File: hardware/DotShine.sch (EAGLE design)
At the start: 55 parts, among them CN1 1X4-BIG, IC1 CAT24M010TS, IC3 SI1145, J3 USB-MICROB, U1 ATMEGA328P-MU-QFN32, U2 TMP102, U3 ATSHA204-TSU, X2 MC-RTC-RV-4162-C7-I2C, X3 S4B-ZR

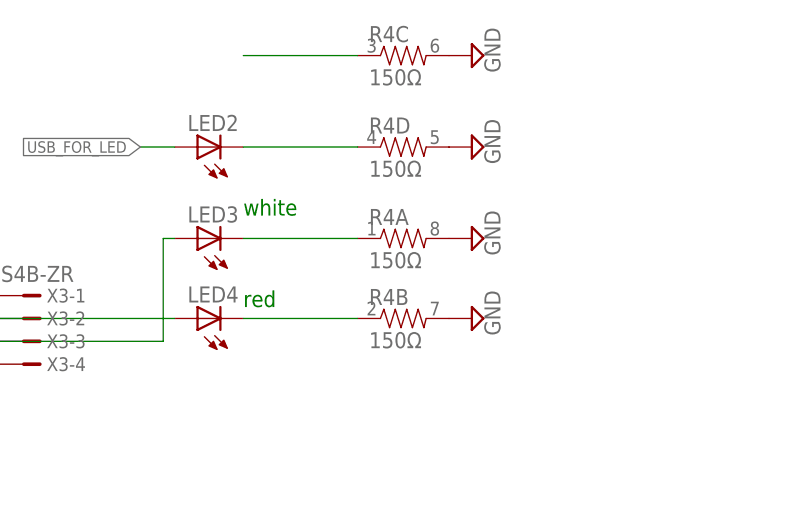
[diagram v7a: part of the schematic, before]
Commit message: Remove IXYS SLMD121H9L solar cell 45mA@4.5V, use small cell and i2c micro crystal
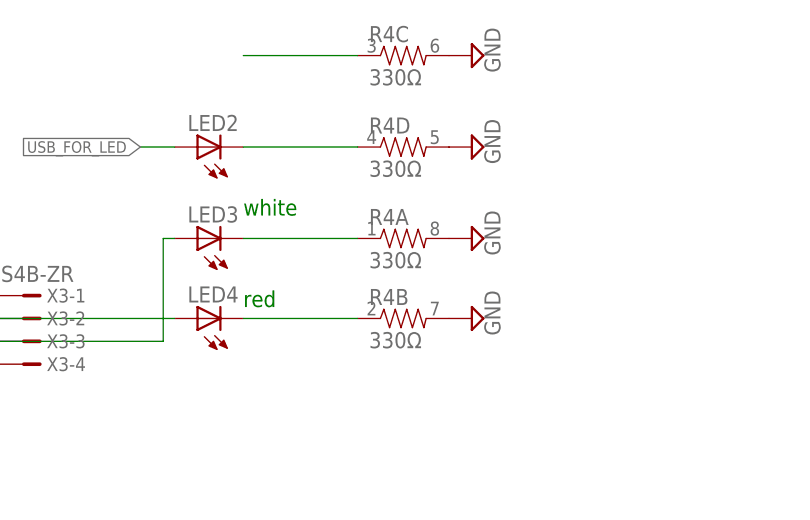
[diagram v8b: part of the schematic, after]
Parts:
- R4: value 150Ω -> 330Ω
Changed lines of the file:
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@@
 <setting verticaltext="up"/>
 </settings>
-<grid distance="0.05" unitdist="inch" unit="inch" style="lines" multiple="1" display="no" altdistance="0.01" altunitdist="inch" altunit="inch"/>
+<grid distance="0.1" unitdist="inch" unit="inch" style="lines" multiple="1" display="no" altdistance="0.01" altunitdist="inch" altunit="inch"/>
 <layers>
 <layer number="1" name="Top" color="4" fill="1" visible="no" active="no"/>
@@
 <part name="SUPPLY11" library="supply2" deviceset="GND" device=""/>
 <part name="+3V7" library="supply1" deviceset="+3V3" device=""/>
-<part name="R4" library="SparkFun" deviceset="RESISTOR-ARRAY" device="0603-ARV" value="150Ω"/>
+<part name="R4" library="SparkFun" deviceset="RESISTOR-ARRAY" device="0603-ARV" value="330Ω"/>
 <part name="SUPPLY12" library="supply2" deviceset="GND" device=""/>
 <part name="SUPPLY27" library="supply2" deviceset="GND" device=""/>
